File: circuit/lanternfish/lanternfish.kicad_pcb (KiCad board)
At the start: 2 copper layers, 100 x 70 mm, 64 parts, among them J1 Input, J2 Prog, J3 Output, Q1 FQD17P06TM, Q2 PSMN5R6-60YLX, Q3 SI2302DDS-T1-GE3, SW1 SW_Push, SW2 SW_Push, SW3 PEC11R-4215F-S0024, SW4 SW_Push, SW5 SW_Push, SW6 SW_SPST, U1 MCP7940N-xMS, U2 L7805, U3 ATmega328PB-AU, Y1 ABS25-32.768KHZ-6-1-T

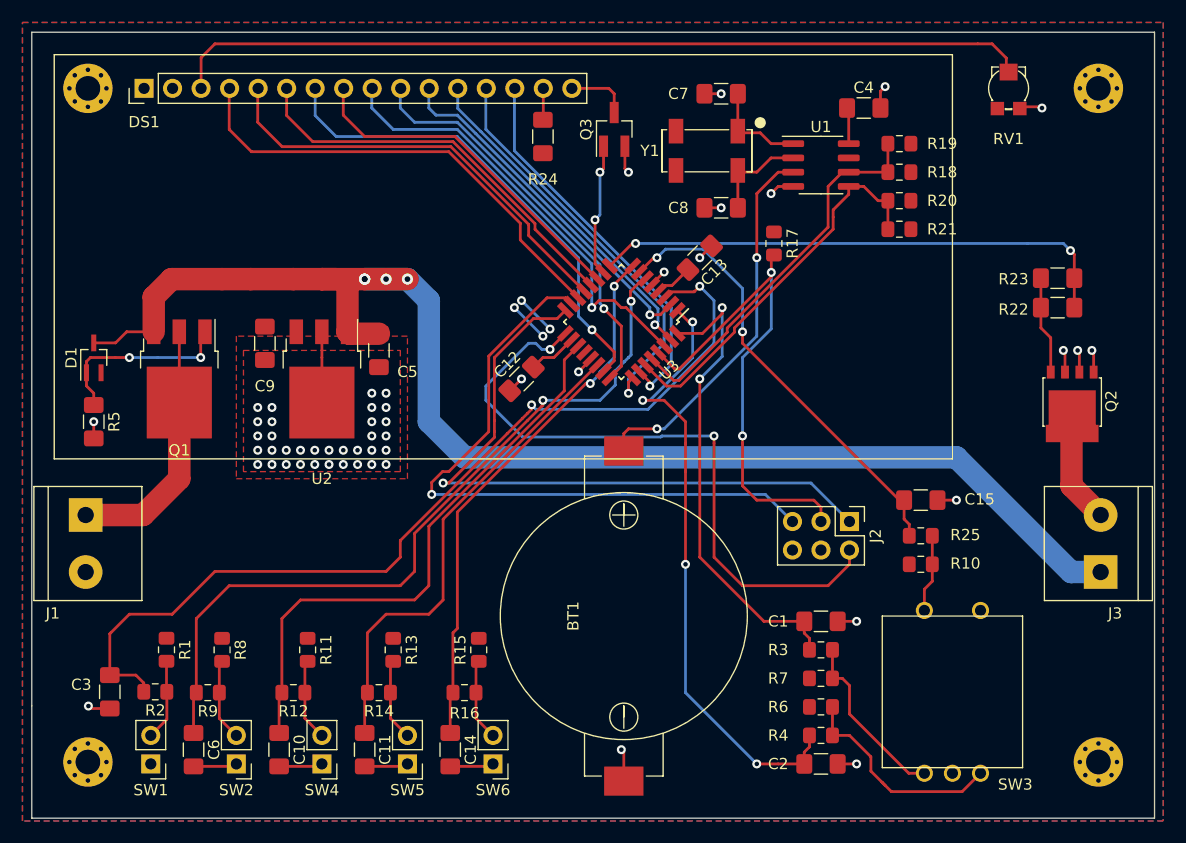
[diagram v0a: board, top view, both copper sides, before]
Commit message: Updated PCB
Added mounting hole + rounded corners
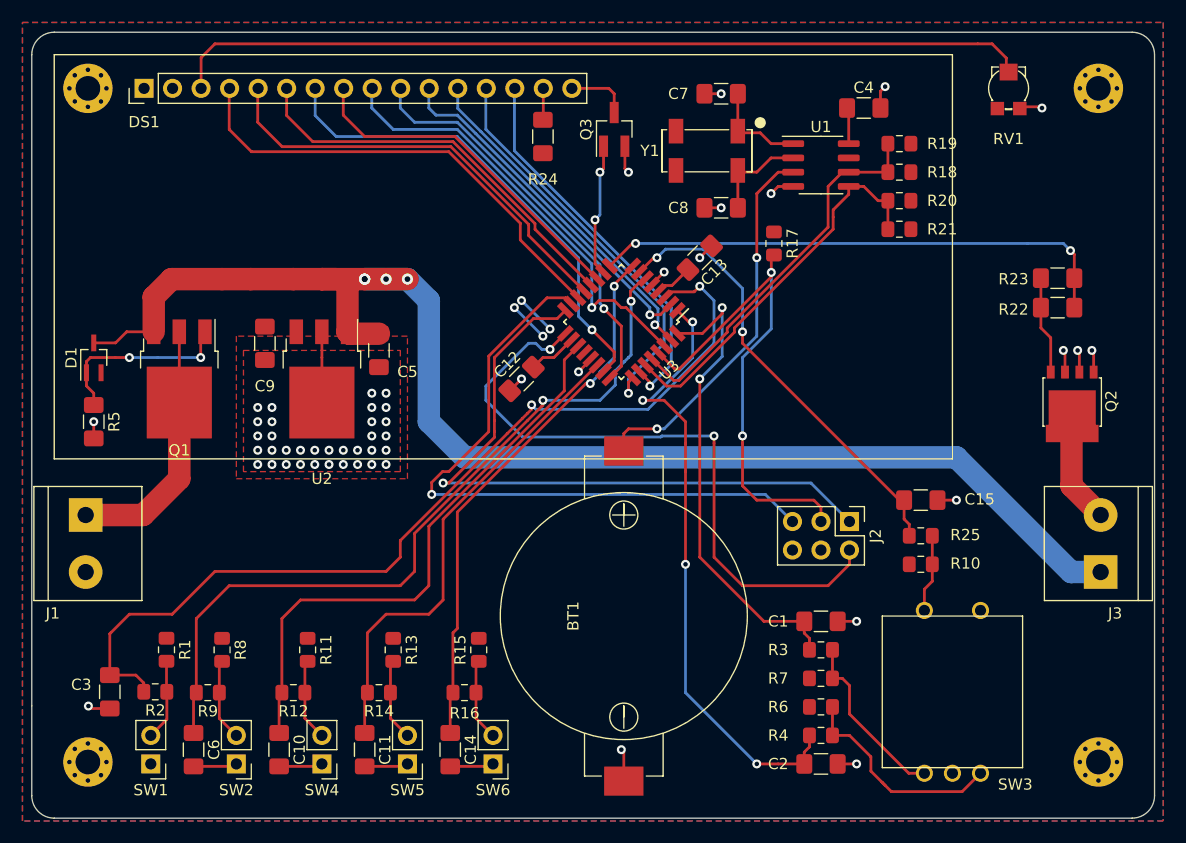
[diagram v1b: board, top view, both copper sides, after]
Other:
- outline, holes or cut-outs redrawn
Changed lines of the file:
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@@
   (general
     (thickness 1.6)
-    (drawings 6)
+    (drawings 12)
     (tracks 569)
     (zones 0)
@@
     (pad_to_mask_clearance 0.05)
     (aux_axis_origin 0 0)
+    (grid_origin 101 130)
     (visible_elements 7FFFFFFF)
     (pcbplotparams
@@
       (effects (font (size 1 1) (thickness 0.15)))
     )
-    (fp_text user %R (at 27.05 3 180) (layer F.Fab)
-      (effects (font (size 1 1) (thickness 0.15)))
-    )
     (fp_line (start 9.27 4.33) (end 47.43 4.33) (layer F.SilkS) (width 0.12))
     (fp_line (start 47.37 4.27) (end 7.365 4.27) (layer F.Fab) (width 0.1))
@@
     (fp_line (start 80 36) (end 0 36) (layer F.SilkS) (width 0.12))
     (fp_line (start 0 36) (end 0 0) (layer F.SilkS) (width 0.12))
+    (fp_text user %R (at 27.05 3 180) (layer F.Fab)
+      (effects (font (size 1 1) (thickness 0.15)))
+    )
     (pad 2 thru_hole oval (at 10.54 3 90) (size 1.7 1.7) (drill 1) (layers *.Cu *.Mask)
       (net 6 +5V))
@@
       (net 10 "Net-(C8-Pad1)"))
   )
-  (gr_line (start 201 130) (end 201 120) (layer Edge.Cuts) (width 0.05))
-  (gr_line (start 101 130) (end 201 130) (layer Edge.Cuts) (width 0.05))
-  (gr_line (start 101 120) (end 101 130) (layer Edge.Cuts) (width 0.05))
-  (gr_line (start 101 120) (end 101 60) (layer Edge.Cuts) (width 0.05))
-  (gr_line (start 201 60) (end 201 120) (layer Edge.Cuts) (width 0.05))
-  (gr_line (start 101 60) (end 201 60) (layer Edge.Cuts) (width 0.05))
+  (gr_circle (center 106 125) (end 111 125.2) (layer Dwgs.User) (width 0.15))
+  (dimension 19.380003 (width 0.15) (layer Dwgs.User)
+    (gr_text "19,380 mm" (at 93.695209 120.31387 270.0295644) (layer Dwgs.User)
+      (effects (font (size 1 1) (thickness 0.15)))
+    )
+    (feature1 (pts (xy 101.2 130) (xy 94.413788 130.003502)))
+    (feature2 (pts (xy 101.19 110.62) (xy 94.403788 110.623502)))
+    (crossbar (pts (xy 94.990209 110.623199) (xy 95.000209 130.003199)))
+    (arrow1a (pts (xy 95.000209 130.003199) (xy 94.413207 128.876998)))
+    (arrow1b (pts (xy 95.000209 130.003199) (xy 95.586048 128.876393)))
+    (arrow2a (pts (xy 94.990209 110.623199) (xy 94.40437 111.750005)))
+    (arrow2b (pts (xy 94.990209 110.623199) (xy 95.577211 111.7494)))
+  )
+  (gr_arc (start 103 128) (end 101 128) (angle -90) (layer Edge.Cuts) (width 0.05))
+  (gr_arc (start 103 62) (end 103 60) (angle -90) (layer Edge.Cuts) (width 0.05))
+  (gr_arc (start 199 62) (end 201 62) (angle -90) (layer Edge.Cuts) (width 0.05))
+  (gr_arc (start 199 128) (end 199 130) (angle -90) (layer Edge.Cuts) (width 0.05))
+  (gr_line (start 201 128) (end 201 120) (layer Edge.Cuts) (width 0.05))
+  (gr_line (start 103 130) (end 199 130) (layer Edge.Cuts) (width 0.05))
+  (gr_line (start 101 120) (end 101 128) (layer Edge.Cuts) (width 0.05))
+  (gr_line (start 101 120) (end 101 62) (layer Edge.Cuts) (width 0.05))
+  (gr_line (start 201 62) (end 201 120) (layer Edge.Cuts) (width 0.05))
+  (gr_line (start 103 60) (end 199 60) (layer Edge.Cuts) (width 0.05))
   (segment (start 153.73 97.3) (end 153.73 95.74) (width 0.25) (layer F.Cu) (net 1))
   (segment (start 153.73 95.74) (end 154.145 95.325) (width 0.25) (layer F.Cu) (net 1))

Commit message: Updated circuit [wip]
Removed 2 switches, connected MFP from RTC to MCU
Updated 25V netclass
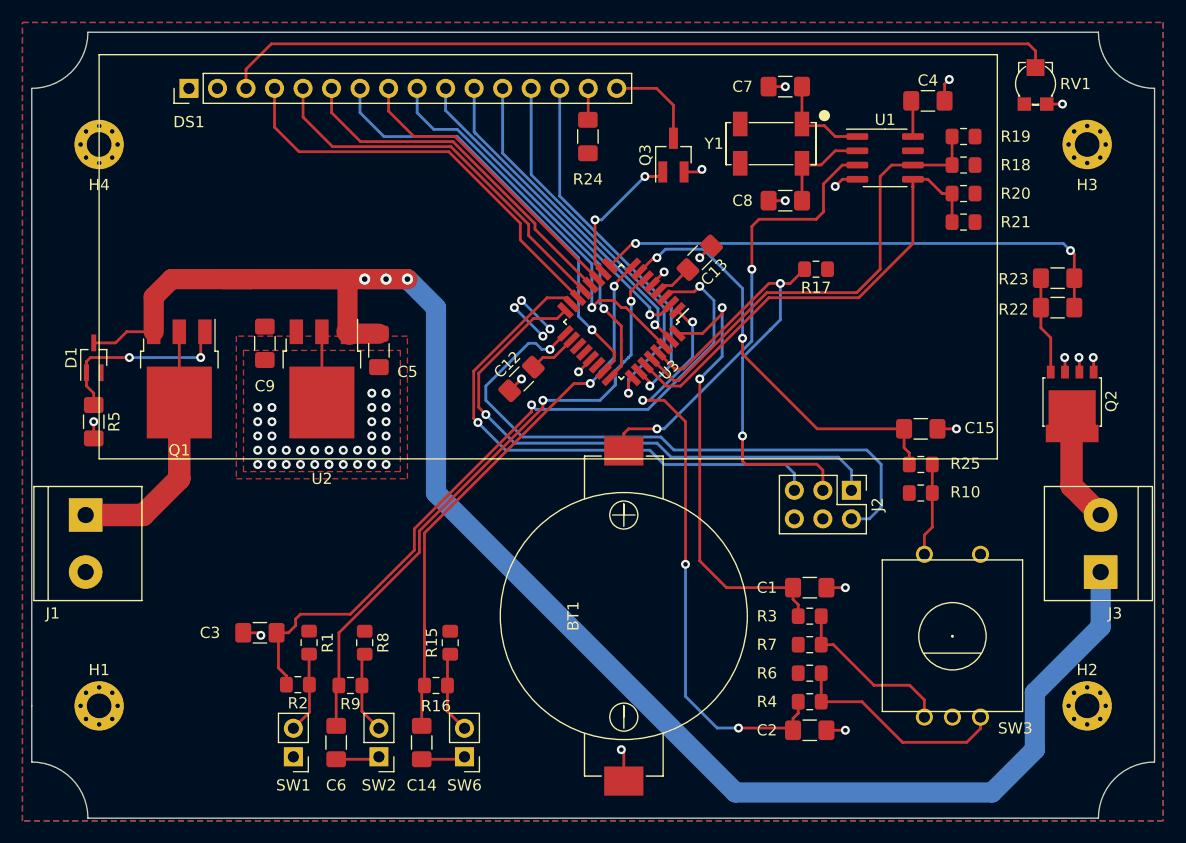
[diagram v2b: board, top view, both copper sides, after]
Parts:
- removed C10, C11: 10uF, Capacitor_SMD:C_1206_3216Metric_Pad1.42x1.75mm_HandSolder
- removed R11, R12, R13, R14: 10kR, Resistor_SMD:R_0805_2012Metric_Pad1.15x1.40mm_HandSolder
- removed REF** (x4): MountingHole_2.2mm_M2_Pad_Via, MountingHole:MountingHole_2.2mm_M2_Pad_Via
- removed SW4, SW5: SW_Push, Connector_PinHeader_2.54mm:PinHeader_1x02_P2.54mm_Vertical
- added H1: MountingHole, MountingHole:MountingHole_2.2mm_M2_Pad_Via, F.Cu at (107.0, 120.0)
- added H2: MountingHole, MountingHole:MountingHole_2.2mm_M2_Pad_Via, F.Cu at (195.0, 120.0)
- added H3: MountingHole, MountingHole:MountingHole_2.2mm_M2_Pad_Via, F.Cu at (195.0, 70.0)
- added H4: MountingHole, MountingHole:MountingHole_2.2mm_M2_Pad_Via, F.Cu at (107.0, 70.0)
- BT1: value Battery_Cell -> CR2032
- moved C3 14.4 mm to (121.3, 113.5), turned to 180 degrees
- moved C6 12.7 mm to (128.1, 123.3)
- moved R1 12.7 mm to (125.7, 114.4)
- moved R2 12.7 mm to (124.7, 118.1)
- moved R8 12.7 mm to (130.7, 114.4)
- moved SW1 12.7 mm to (124.3, 124.5)
- moved R9 12.7 mm to (129.4, 118.2)
- moved SW2 12.7 mm to (131.9, 124.5)
- moved C15 6.35 mm to (180.2, 95.3)
- moved R10 6.35 mm to (180.2, 101.0)
- moved R25 6.35 mm to (180.2, 98.5)
- moved Q3 5.75 mm to (158.2, 70.9)
- moved C4 5.75 mm to (180.8, 66.1)
- moved C7 5.75 mm to (168.1, 64.8)
- moved C8 5.75 mm to (168.1, 75.0)
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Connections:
- U1 pad 7: Net-(U1-Pad7) -> /RTC_MSP
- U3 pad 19: /SW3 -> /RTC_MSP
- U3 pad 22: /SW4 -> Net-(U3-Pad22)
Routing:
- net /SW3: track 51.4 -> 0.00 mm
- net /SW4: track 43.6 -> 0.00 mm
- net VDD: track 123.4 -> 151.3 mm, vias 4 -> 3
- net /SW1: track 82.9 -> 66.3 mm
- net /SW2: track 69.2 -> 55.4 mm
- net GND: track 57.8 -> 46.0 mm
- net /MOSI: track 57.7 -> 48.3 mm
- net /SCL: track 34.4 -> 43.4 mm
- net /MISO: track 59.0 -> 50.4 mm
- net /SDA: track 34.4 -> 42.2 mm
- net Net-(R13-Pad2): track 7.32 -> 0.00 mm
- net Net-(R11-Pad2): track 7.32 -> 0.00 mm
- net +BATT: track 33.7 -> 39.7 mm
- net /LCD_RW: track 38.9 -> 34.6 mm
- net /LCD_D1: track 31.0 -> 26.8 mm
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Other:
- outline, holes or cut-outs redrawn
- net class 25V: trace_width 2 -> 1.8
